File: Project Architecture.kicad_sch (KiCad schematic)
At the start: 0 parts

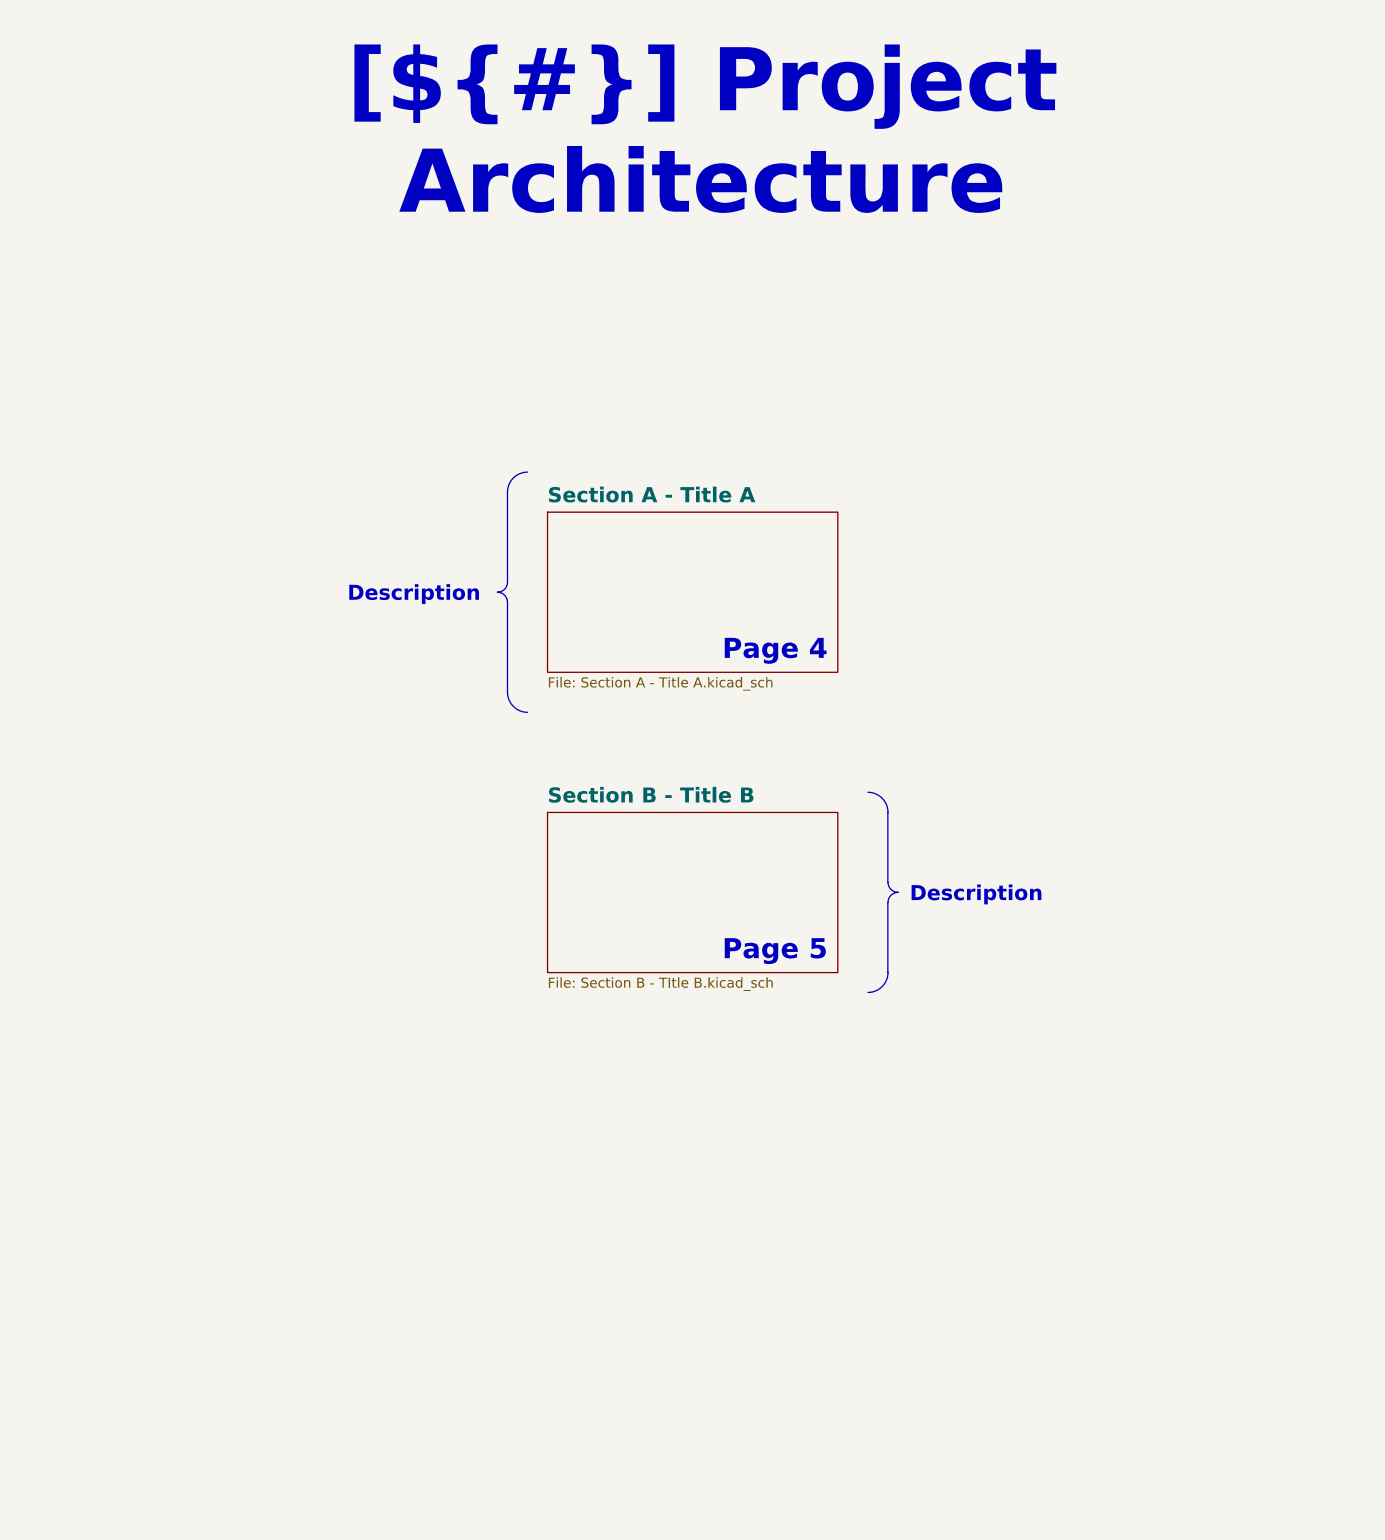
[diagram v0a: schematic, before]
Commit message: Initial commit: Moved over previous design and added isolation to CAN bus.
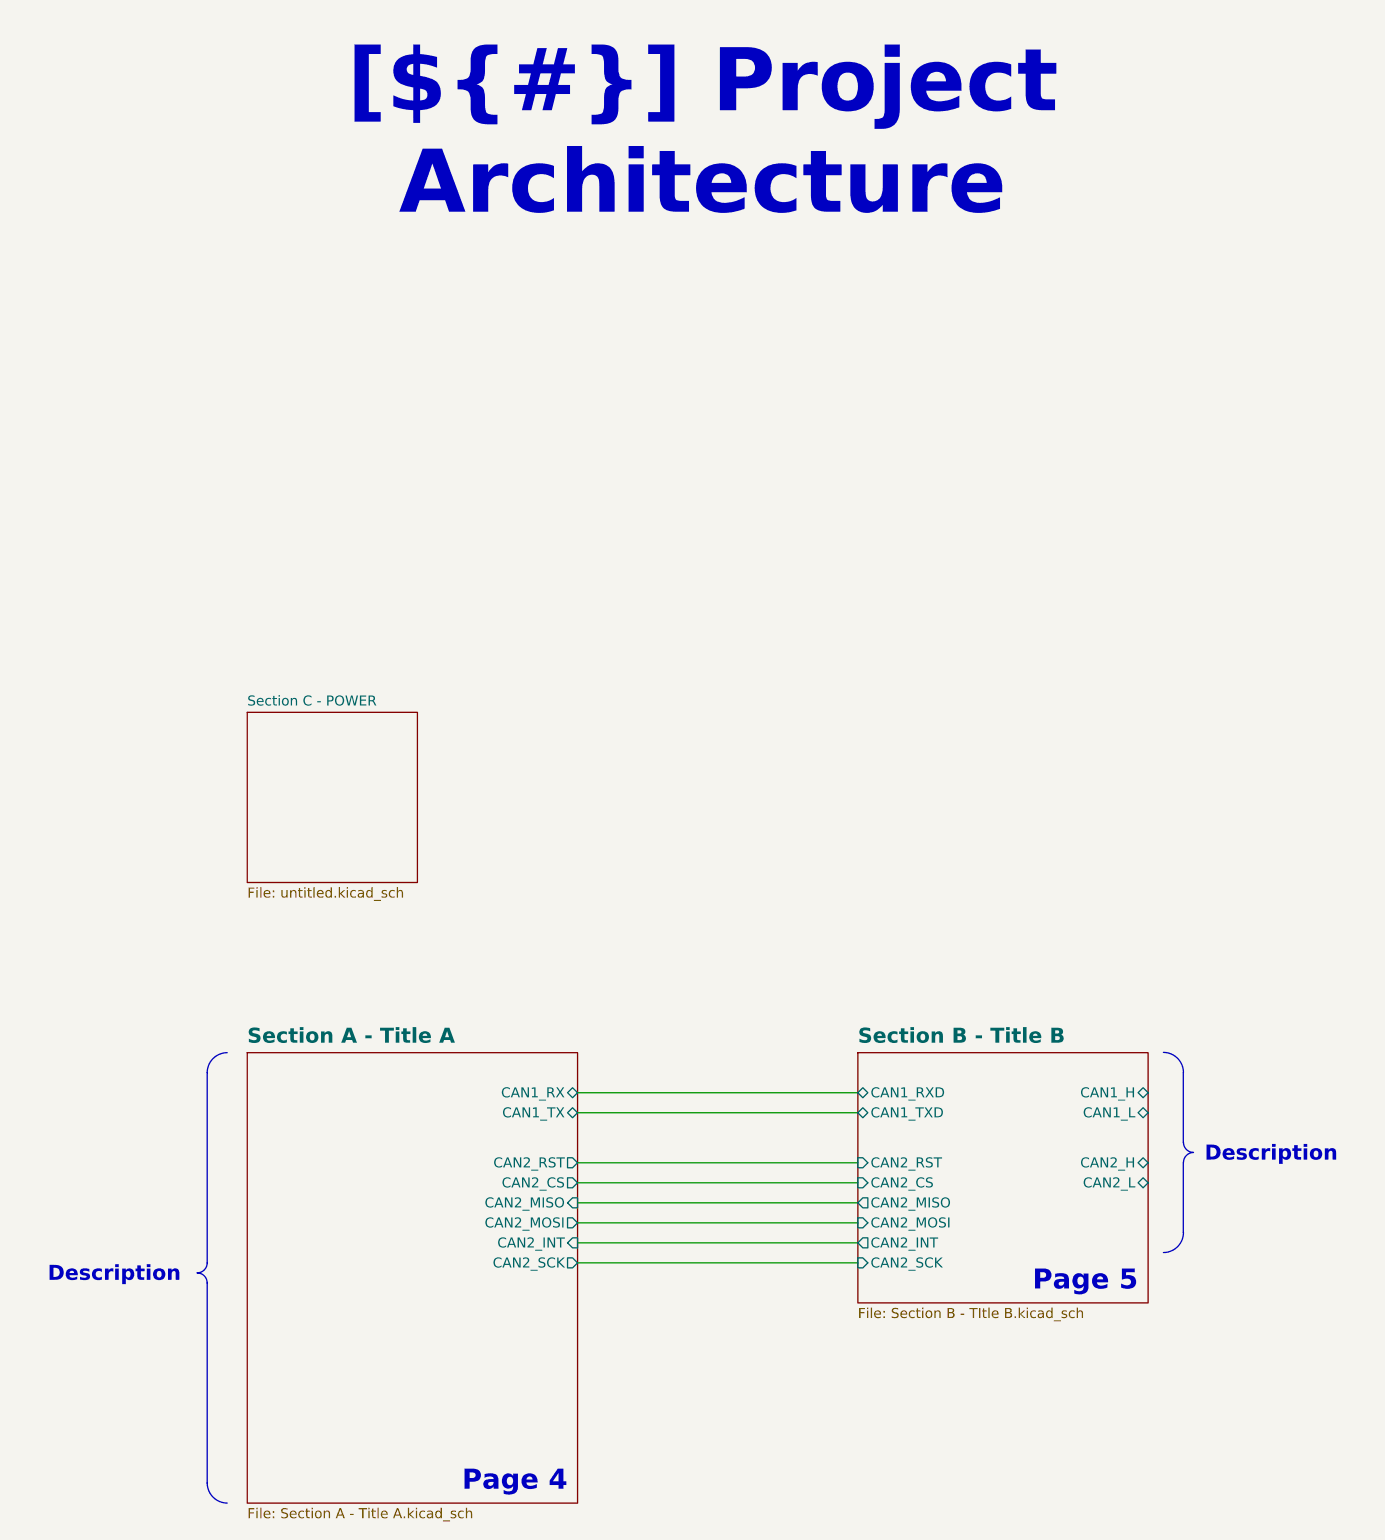
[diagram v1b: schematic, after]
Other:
- added sheet Section C - POWER (untitled.kicad_sch)
- sheet Section A - Title A ports: added CAN1_RX, CAN1_TX, CAN2_CS, CAN2_INT, CAN2_MISO, CAN2_MOSI, CAN2_RST, CAN2_SCK; removed none
- sheet Section B - Title B ports: added CAN1_H, CAN1_L, CAN1_RXD, CAN1_TXD, CAN2_CS, CAN2_H, CAN2_INT, CAN2_L, CAN2_MISO, CAN2_MOSI, CAN2_RST, CAN2_SCK; removed none
